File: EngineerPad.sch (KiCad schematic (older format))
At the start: 67 parts, among them J1 AVR ISP, SW1 SW_Push, SW10 SW_Push, SW11 SW_Push, SW12 SW_Push, SW13 SW_Push, SW14 SW_Push, SW15 SW_Push, SW16 SW_Push, SW17 SW_Push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

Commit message: switch to type a receptacle
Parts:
- removed Boot1: Boot, Button_Switch_THT:SW_PUSH_6mm, symbol Switch:SW_Push
- removed R3, R4: 5.1K, Resistor_THT:R_Axial_DIN0204_L3.6mm_D1.6mm_P5.08mm_Horizontal, symbol Device:R
- removed USB1: TYPE-C, JSA:USB_C_Receptacle_HRO_TYPE-C-31-M-12, symbol JSA:USB-2.0-Type-C-Receptacle
- added J2: USB_A, Connector_USB:USB_A_CONNFLY_DS1095-WNR0, symbol Connector:USB_A
- F1: footprint Fuse:Fuse_Bourns_MF-RG500 -> Fuse:Fuse_Bourns_MF-RHT050
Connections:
- net labels removed: Boot, CC1, CC2, DN, DP, VSUB
- wire segments 105 -> 86
- no-connect marks 7 -> 6

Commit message: socket and low profile
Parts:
- SW21, SW22, SW23: footprint Button_Switch_Keyboard:SW_Cherry_MX_1.00u_PCB -> JSA:SW_PG1350
- U1: footprint Package_DIP:DIP-28_W7.62mm -> Package_DIP:DIP-28_W7.62mm_Socket
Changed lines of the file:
@@
 F 0 "U1" H 1206 3746 50  0000 R CNN
 F 1 "ATmega328P-PU" H 1206 3655 50  0000 R CNN
-F 2 "Package_DIP:DIP-28_W7.62mm" H 1850 3700 50  0001 C CIN
+F 2 "Package_DIP:DIP-28_W7.62mm_Socket" H 1850 3700 50  0001 C CIN
 F 3 "http://ww1.microchip.com/downloads/en/DeviceDoc/ATmega328_P%20AVR%20MCU%20with%20picoPower%20Technology%20Data%20Sheet%2040001984A.pdf" H 1850 3700 50  0001 C CNN
 	1    1850 3700
@@
 F 0 "SW23" H 10550 4685 50  0000 C CNN
 F 1 "SW_Push" H 10550 4594 50  0000 C CNN
-F 2 "Button_Switch_Keyboard:SW_Cherry_MX_1.00u_PCB" H 10550 4600 50  0001 C CNN
+F 2 "JSA:SW_PG1350" H 10550 4600 50  0001 C CNN
 F 3 "~" H 10550 4600 50  0001 C CNN
 	1    10550 4400
@@
 F 0 "SW22" H 10050 4685 50  0000 C CNN
 F 1 "SW_Push" H 10050 4594 50  0000 C CNN
-F 2 "Button_Switch_Keyboard:SW_Cherry_MX_1.00u_PCB" H 10050 4600 50  0001 C CNN
+F 2 "JSA:SW_PG1350" H 10050 4600 50  0001 C CNN
 F 3 "~" H 10050 4600 50  0001 C CNN
 	1    10050 4400
@@
 F 0 "SW21" H 9550 4685 50  0000 C CNN
 F 1 "SW_Push" H 9550 4594 50  0000 C CNN
-F 2 "Button_Switch_Keyboard:SW_Cherry_MX_1.00u_PCB" H 9550 4600 50  0001 C CNN
+F 2 "JSA:SW_PG1350" H 9550 4600 50  0001 C CNN
 F 3 "~" H 9550 4600 50  0001 C CNN
 	1    9550 4400

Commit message: first layout
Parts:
- added R3: 1.5k, Resistor_THT:R_Axial_DIN0204_L3.6mm_D1.6mm_P5.08mm_Horizontal, symbol Device:R
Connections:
- net SCK is gone; now on net Row0: J1.3 (SCK), U1.19 (PB5)
- net SDI is gone; now on net Row2: J1.4 (SDI), U1.17 (PB3)
- net SDO is gone; now on net Row1: J1.1 (SDO), U1.18 (PB4)
- net +5V: now also R3.1
- net Col0: now also U1.27 (PC4); no longer U1.23 (PC0)
- net Col1: now also U1.26 (PC3); no longer U1.24 (PC1)
- net Col3: now also U1.24 (PC1); no longer U1.26 (PC3)
- net Col4: now also U1.23 (PC0); no longer U1.27 (PC4)
- net D+: now also U1.5 (PD3); no longer U1.4 (PD2)
- net D-: now also U1.4 (PD2); no longer U1.5 (PD3)
- net Row0: no longer U1.2 (PD0)
- net Row1: no longer U1.3 (PD1)
- net Row2: no longer U1.6 (PD4)
- net Row3: now also U1.16 (PB2); no longer U1.12 (PD6)
- net Row4: now also U1.15 (PB1); no longer U1.13 (PD7)
- net DN: now reaches D25.1 (K), J2.2 (D-), R2.2
- net DN: now also R3.2
- net DP: now reaches D24.1 (K), J2.3 (D+), R1.2
- no-connect marks 6 -> 10
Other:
- moved on the sheet: D25, R1, R2
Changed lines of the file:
@@
 $EndComp
 Text GLabel 4400 5200 2    50   Input ~ 0
-SCK
+Row0
 Text GLabel 4400 5100 2    50   Input ~ 0
-SDI
-Text GLabel 4400 5000 2    50   Input ~ 0
-SDO
-Text GLabel 2450 3000 2    50   Input ~ 0
-SCK
-Text GLabel 2450 2900 2    50   Input ~ 0
-SDO
+Row2
+Text GLabel 2450 2700 2    50   Input ~ 0
+Row3
 Text GLabel 2450 2800 2    50   Input ~ 0
-SDI
+Row2
 $Comp
 L power:+5V #PWR09
@@
 Col0
 Connection ~ 8850 1350
-Text GLabel 2450 4200 2    50   Input ~ 0
+Text GLabel 2450 3000 2    50   Input ~ 0
 Row0
-Text GLabel 2450 4300 2    50   Input ~ 0
+Text GLabel 2450 2900 2    50   Input ~ 0
 Row1
-Text GLabel 2450 3400 2    50   Input ~ 0
+Text GLabel 2450 3800 2    50   Input ~ 0
 Col0
-Text GLabel 2450 3500 2    50   Input ~ 0
+Text GLabel 2450 3700 2    50   Input ~ 0
 Col1
 NoConn ~ 2450 2500
-NoConn ~ 2450 2600
-NoConn ~ 2450 2700
 NoConn ~ 1250 2500
+Text GLabel 2450 4500 2    50   Input ~ 0
+D+
 Text GLabel 2450 4400 2    50   Input ~ 0
-D+
-Text GLabel 2450 4500 2    50   Input ~ 0
 D-
 Text Notes 6900 6250 0    50   ~ 0
@@
 Text GLabel 10350 850  1    50   Input ~ 0
 Col4
-Text GLabel 2450 4600 2    50   Input ~ 0
-Row2
-Text GLabel 2450 4800 2    50   Input ~ 0
-Row3
-Text GLabel 2450 4900 2    50   Input ~ 0
+Text GLabel 2450 2600 2    50   Input ~ 0
 Row4
 Text GLabel 2450 3600 2    50   Input ~ 0
 Col2
-Text GLabel 2450 3700 2    50   Input ~ 0
+Text GLabel 2450 3500 2    50   Input ~ 0
 Col3
-Text GLabel 2450 3800 2    50   Input ~ 0
+Text GLabel 2450 3400 2    50   Input ~ 0
 Col4
 Connection ~ 8350 1350
@@
 L Device:R R1
 U 1 1 5F4818C7
-P 6200 1850
-F 0 "R1" V 5993 1850 50  0000 C CNN
-F 1 "75" V 6084 1850 50  0000 C CNN
-F 2 "Resistor_THT:R_Axial_DIN0204_L3.6mm_D1.6mm_P5.08mm_Horizontal" V 6130 1850 50  0001 C CNN
-F 3 "~" H 6200 1850 50  0001 C CNN
-	1    6200 1850
+P 6550 1850
+F 0 "R1" V 6343 1850 50  0000 C CNN
+F 1 "75" V 6434 1850 50  0000 C CNN
+F 2 "Resistor_THT:R_Axial_DIN0204_L3.6mm_D1.6mm_P5.08mm_Horizontal" V 6480 1850 50  0001 C CNN
+F 3 "~" H 6550 1850 50  0001 C CNN
+	1    6550 1850
 	0    1    1    0
 $EndComp
@@
 L Device:R R2
 U 1 1 5F48290F
-P 6450 1950
-F 0 "R2" V 6243 1950 50  0000 C CNN
-F 1 "75" V 6334 1950 50  0000 C CNN
-F 2 "Resistor_THT:R_Axial_DIN0204_L3.6mm_D1.6mm_P5.08mm_Horizontal" V 6380 1950 50  0001 C CNN
-F 3 "~" H 6450 1950 50  0001 C CNN
-	1    6450 1950
+P 6800 1950
+F 0 "R2" V 6593 1950 50  0000 C CNN
+F 1 "75" V 6684 1950 50  0000 C CNN
+F 2 "Resistor_THT:R_Axial_DIN0204_L3.6mm_D1.6mm_P5.08mm_Horizontal" V 6730 1950 50  0001 C CNN
+F 3 "~" H 6800 1950 50  0001 C CNN
+	1    6800 1950
 	0    1    1    0
 $EndComp
@@
 	5650 1850 5950 1850
 Wire Wire Line
-	5650 1950 6250 1950
-Wire Wire Line
-	6350 1850 6900 1850
-Text GLabel 6900 1850 2    50   Input ~ 0
+	6700 1850 7250 1850
+Text GLabel 7250 1850 2    50   Input ~ 0
 D+
-Text GLabel 7100 1950 2    50   Input ~ 0
+Text GLabel 7450 1950 2    50   Input ~ 0
 D-
 Wire Wire Line
-	6600 1950 7100 1950
+	6950 1950 7450 1950
 $Comp
 L Device:D_Zener D25
 U 1 1 5F49960F
-P 6250 2100
-F 0 "D25" V 6204 2180 50  0000 L CNN
-F 1 "3.6V" V 6295 2180 50  0000 L CNN
-F 2 "Diode_THT:D_DO-35_SOD27_P7.62mm_Horizontal" H 6250 2100 50  0001 C CNN
-F 3 "~" H 6250 2100 50  0001 C CNN
-	1    6250 2100
+P 6600 2100
+F 0 "D25" V 6554 2180 50  0000 L CNN
+F 1 "3.6V" V 6645 2180 50  0000 L CNN
+F 2 "Diode_THT:D_DO-35_SOD27_P7.62mm_Horizontal" H 6600 2100 50  0001 C CNN
+F 3 "~" H 6600 2100 50  0001 C CNN
+	1    6600 2100
 	0    1    1    0
 $EndComp
@@
 	5950 2150 5950 2250
 Connection ~ 5950 1850
-Wire Wire Line
-	5950 1850 6050 1850
-Connection ~ 6250 1950
-Wire Wire Line
-	6250 1950 6300 1950
+Connection ~ 6600 1950
+Wire Wire Line
+	6600 1950 6650 1950
 Wire Wire Line
 	5250 2250 5350 2250
@@
 Connection ~ 5350 2250
 Connection ~ 5950 2250
-Wire Wire Line
-	5950 2250 6250 2250
 Wire Wire Line
 	5700 2250 5700 2400
@@
 Wire Wire Line
 	5800 1250 5800 1650
+Wire Wire Line
+	5800 1650 6050 1650
+$Comp
+L Device:R R3
+U 1 1 5F481387
+P 6300 1500
+F 0 "R3" H 6370 1546 50  0000 L CNN
+F 1 "1.5k" H 6370 1455 50  0000 L CNN
+F 2 "Resistor_THT:R_Axial_DIN0204_L3.6mm_D1.6mm_P5.08mm_Horizontal" V 6230 1500 50  0001 C CNN
+F 3 "~" H 6300 1500 50  0001 C CNN
+	1    6300 1500
+	1    0    0    -1
+$EndComp
+Wire Wire Line
+	5650 1950 6300 1950
+Wire Wire Line
+	5950 1850 6400 1850
+Wire Wire Line
+	5950 2250 6600 2250
+Wire Wire Line
+	6300 1650 6300 1950
+Connection ~ 6300 1950
+Wire Wire Line
+	6300 1950 6600 1950
+Wire Wire Line
+	6300 1350 6050 1350
+Connection ~ 6050 1350
 Connection ~ 5800 1650
-Wire Wire Line
-	5800 1650 6050 1650
+Text Label 5750 1850 0    50   ~ 0
+DP
+Text Label 5750 1950 0    50   ~ 0
+DN
+NoConn ~ 2450 4900
+NoConn ~ 9150 5350
+Text GLabel 4400 5000 2    50   Input ~ 0
+Row1
+NoConn ~ 2450 4200
+NoConn ~ 2450 4300
+NoConn ~ 2450 4600
+NoConn ~ 2450 4800
 $EndSCHEMATC

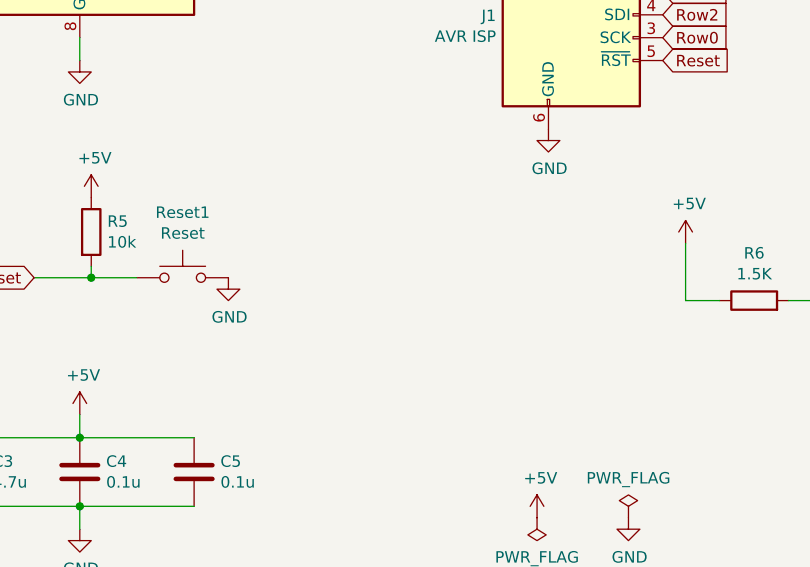
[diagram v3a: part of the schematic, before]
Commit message: Form factor 因為要做成5mm邊框切齊鍵帽，因此PCB從鍵帽處內縮1mm，外殼預計是5mm。
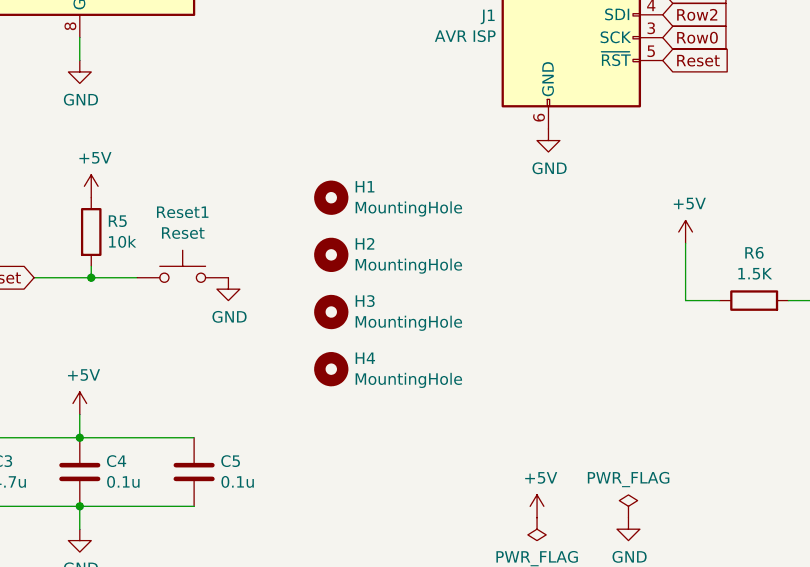
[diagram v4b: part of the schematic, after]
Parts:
- added H1, H2, H3, H4: MountingHole, MountingHole:MountingHole_2.2mm_M2, symbol Mechanical:MountingHole
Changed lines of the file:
@@
 Text GLabel 4400 5300 2    50   Input ~ 0
 Reset
-$Comp
-L JSA:Oshwa_ISP_6 J1
-U 1 1 5F1679A9
-P 4000 5200
-F 0 "J1" H 3671 5296 50  0000 R CNN
-F 1 "AVR ISP" H 3671 5205 50  0000 R CNN
-F 2 "JSA:AVRISP" V 3750 5250 50  0001 C CNN
-F 3 "https://www.oshwa.org/a-resolution-to-redefine-spi-signal-names" H 2725 4650 50  0001 C CNN
-	1    4000 5200
-	1    0    0    -1
-$EndComp
 Text GLabel 4400 5200 2    50   Input ~ 0
 Row0
@@
 NoConn ~ 2450 4600
 NoConn ~ 2450 4800
+$Comp
+L JSA:Oshwa_ISP_6 J1
+U 1 1 5F1679A9
+P 4000 5200
+F 0 "J1" H 3671 5296 50  0000 R CNN
+F 1 "AVR ISP" H 3671 5205 50  0000 R CNN
+F 2 "JSA:AVRISP" V 3750 5250 50  0001 C CNN
+F 3 "https://www.oshwa.org/a-resolution-to-redefine-spi-signal-names" H 2725 4650 50  0001 C CNN
+	1    4000 5200
+	1    0    0    -1
+$EndComp
+$Comp
+L Mechanical:MountingHole H1
+U 1 1 5F5595B1
+P 2950 5900
+F 0 "H1" H 3050 5946 50  0000 L CNN
+F 1 "MountingHole" H 3050 5855 50  0000 L CNN
+F 2 "MountingHole:MountingHole_2.2mm_M2" H 2950 5900 50  0001 C CNN
+F 3 "~" H 2950 5900 50  0001 C CNN
+	1    2950 5900
+	1    0    0    -1
+$EndComp
+$Comp
+L Mechanical:MountingHole H2
+U 1 1 5F55F584
+P 2950 6150
+F 0 "H2" H 3050 6196 50  0000 L CNN
+F 1 "MountingHole" H 3050 6105 50  0000 L CNN
+F 2 "MountingHole:MountingHole_2.2mm_M2" H 2950 6150 50  0001 C CNN
+F 3 "~" H 2950 6150 50  0001 C CNN
+	1    2950 6150
+	1    0    0    -1
+$EndComp
+$Comp
+L Mechanical:MountingHole H3
+U 1 1 5F5615B3
+P 2950 6400
+F 0 "H3" H 3050 6446 50  0000 L CNN
+F 1 "MountingHole" H 3050 6355 50  0000 L CNN
+F 2 "MountingHole:MountingHole_2.2mm_M2" H 2950 6400 50  0001 C CNN
+F 3 "~" H 2950 6400 50  0001 C CNN
+	1    2950 6400
+	1    0    0    -1
+$EndComp
+$Comp
+L Mechanical:MountingHole H4
+U 1 1 5F563758
+P 2950 6650
+F 0 "H4" H 3050 6696 50  0000 L CNN
+F 1 "MountingHole" H 3050 6605 50  0000 L CNN
+F 2 "MountingHole:MountingHole_2.2mm_M2" H 2950 6650 50  0001 C CNN
+F 3 "~" H 2950 6650 50  0001 C CNN
+	1    2950 6650
+	1    0    0    -1
+$EndComp
 $EndSCHEMATC

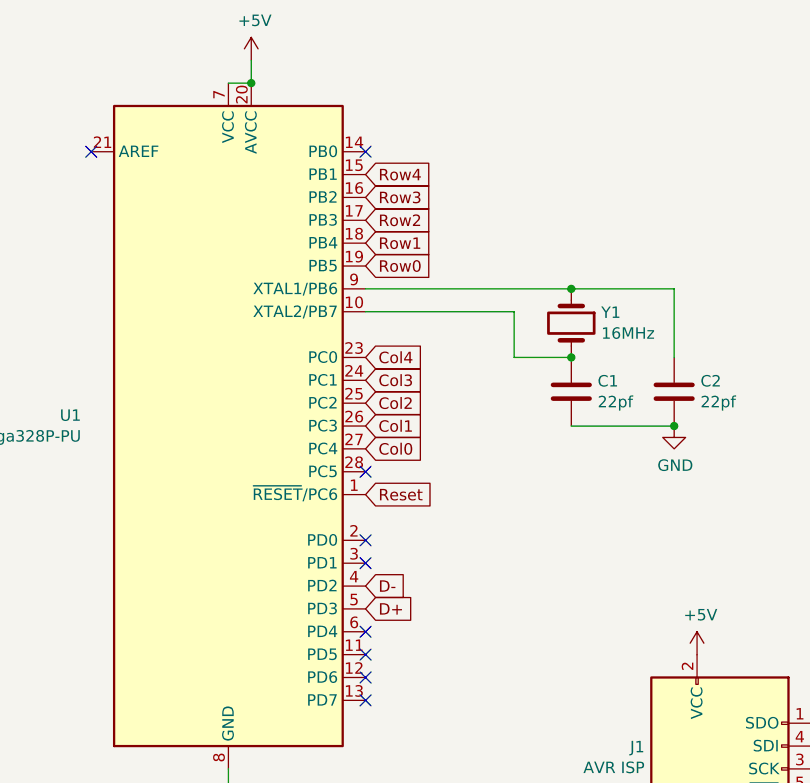
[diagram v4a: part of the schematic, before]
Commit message: inch based design
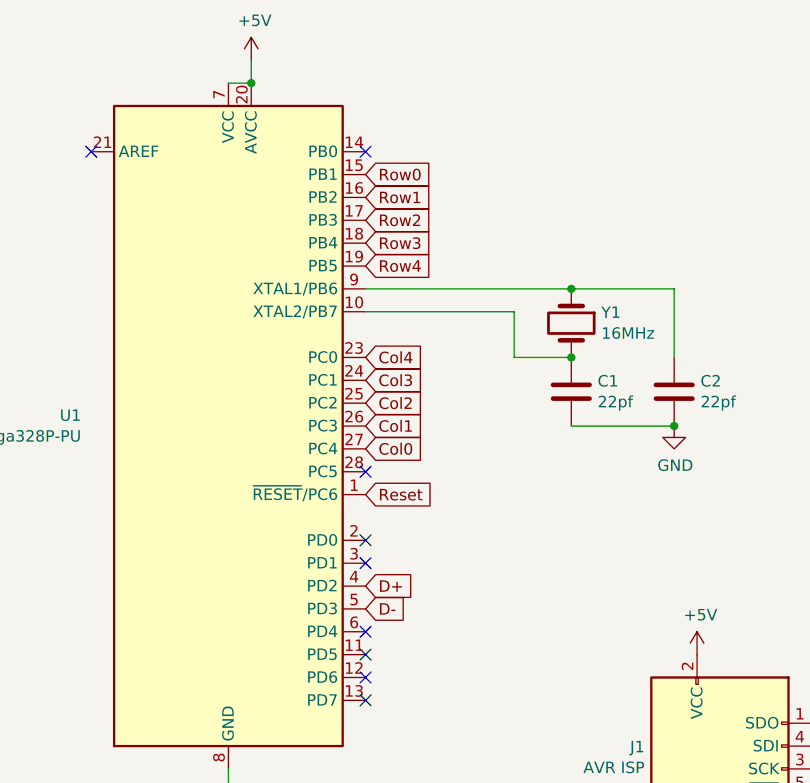
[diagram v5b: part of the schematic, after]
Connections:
- net D+: now also U1.4 (PD2); no longer U1.5 (PD3)
- net D-: now also U1.5 (PD3); no longer U1.4 (PD2)
- net Row0: now also U1.15 (PB1); no longer U1.19 (PB5)
- net Row1: now also U1.16 (PB2); no longer U1.18 (PB4)
- net Row3: now also U1.18 (PB4); no longer U1.16 (PB2)
- net Row4: now also U1.19 (PB5); no longer U1.15 (PB1)
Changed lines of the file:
@@
 Text GLabel 4400 5100 2    50   Input ~ 0
 Row2
-Text GLabel 2450 2700 2    50   Input ~ 0
+Text GLabel 2450 2900 2    50   Input ~ 0
 Row3
 Text GLabel 2450 2800 2    50   Input ~ 0
@@
 Col0
 Connection ~ 8850 1350
-Text GLabel 2450 3000 2    50   Input ~ 0
+Text GLabel 2450 2600 2    50   Input ~ 0
 Row0
-Text GLabel 2450 2900 2    50   Input ~ 0
+Text GLabel 2450 2700 2    50   Input ~ 0
 Row1
 Text GLabel 2450 3800 2    50   Input ~ 0
@@
 NoConn ~ 2450 2500
 NoConn ~ 1250 2500
+Text GLabel 2450 4400 2    50   Input ~ 0
+D+
 Text GLabel 2450 4500 2    50   Input ~ 0
-D+
-Text GLabel 2450 4400 2    50   Input ~ 0
 D-
 Text Notes 6900 6250 0    50   ~ 0
@@
 Text GLabel 10350 850  1    50   Input ~ 0
 Col4
-Text GLabel 2450 2600 2    50   Input ~ 0
+Text GLabel 2450 3000 2    50   Input ~ 0
 Row4
 Text GLabel 2450 3600 2    50   Input ~ 0

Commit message: wip
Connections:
- net Col0: now also J1.3 (SCK), U1.19 (PB5); no longer U1.27 (PC4)
- net Col1: now also J1.1 (SDO), U1.18 (PB4); no longer U1.26 (PC3)
- net Col2: now also J1.4 (SDI), U1.17 (PB3); no longer U1.25 (PC2)
- net Col3: now also U1.16 (PB2); no longer U1.24 (PC1)
- net Col4: now also U1.15 (PB1); no longer U1.23 (PC0)
- net Row0: now also U1.23 (PC0); no longer J1.3 (SCK), U1.15 (PB1)
- net Row1: now also U1.24 (PC1); no longer J1.1 (SDO), U1.16 (PB2)
- net Row2: now also U1.25 (PC2); no longer J1.4 (SDI), U1.17 (PB3)
- net Row3: now also U1.26 (PC3); no longer U1.18 (PB4)
- net Row4: now also U1.27 (PC4); no longer U1.19 (PB5)
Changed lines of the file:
@@
 Reset
 Text GLabel 4400 5200 2    50   Input ~ 0
-Row0
+Col0
 Text GLabel 4400 5100 2    50   Input ~ 0
-Row2
-Text GLabel 2450 2900 2    50   Input ~ 0
+Col2
+Text GLabel 2450 3700 2    50   Input ~ 0
 Row3
-Text GLabel 2450 2800 2    50   Input ~ 0
+Text GLabel 2450 3600 2    50   Input ~ 0
 Row2
 $Comp
@@
 Col0
 Connection ~ 8850 1350
-Text GLabel 2450 2600 2    50   Input ~ 0
+Text GLabel 2450 3400 2    50   Input ~ 0
 Row0
-Text GLabel 2450 2700 2    50   Input ~ 0
+Text GLabel 2450 3500 2    50   Input ~ 0
 Row1
-Text GLabel 2450 3800 2    50   Input ~ 0
+Text GLabel 2450 3000 2    50   Input ~ 0
 Col0
-Text GLabel 2450 3700 2    50   Input ~ 0
+Text GLabel 2450 2900 2    50   Input ~ 0
 Col1
 NoConn ~ 2450 2500
@@
 Text GLabel 10350 850  1    50   Input ~ 0
 Col4
-Text GLabel 2450 3000 2    50   Input ~ 0
+Text GLabel 2450 3800 2    50   Input ~ 0
 Row4
-Text GLabel 2450 3600 2    50   Input ~ 0
+Text GLabel 2450 2800 2    50   Input ~ 0
 Col2
-Text GLabel 2450 3500 2    50   Input ~ 0
+Text GLabel 2450 2700 2    50   Input ~ 0
 Col3
-Text GLabel 2450 3400 2    50   Input ~ 0
+Text GLabel 2450 2600 2    50   Input ~ 0
 Col4
 Connection ~ 8350 1350
@@
 NoConn ~ 9150 5350
 Text GLabel 4400 5000 2    50   Input ~ 0
-Row1
+Col1
 NoConn ~ 2450 4200
 NoConn ~ 2450 4300

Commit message: handwired
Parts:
- added J?: AVR-ISP-6, symbol Connector:AVR-ISP-6
- J1: value AVR ISP -> AVR ISP 6
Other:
- moved on the sheet: J1
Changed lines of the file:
@@
 L power:+5V #PWR04
 U 1 1 5F169608
-P 3900 4700
-F 0 "#PWR04" H 3900 4550 50  0001 C CNN
-F 1 "+5V" H 3915 4873 50  0000 C CNN
-F 2 "" H 3900 4700 50  0001 C CNN
-F 3 "" H 3900 4700 50  0001 C CNN
-	1    3900 4700
-	1    0    0    -1
+P 3400 1700
+F 0 "#PWR04" H 3400 1550 50  0001 C CNN
+F 1 "+5V" H 3415 1873 50  0000 C CNN
+F 2 "" H 3400 1700 50  0001 C CNN
+F 3 "" H 3400 1700 50  0001 C CNN
+	1    3400 1700
+	0    1    1    0
 $EndComp
 $Comp
 L power:GND #PWR07
 U 1 1 5F169EF0
-P 3900 5600
-F 0 "#PWR07" H 3900 5350 50  0001 C CNN
-F 1 "GND" H 3905 5427 50  0000 C CNN
-F 2 "" H 3900 5600 50  0001 C CNN
-F 3 "" H 3900 5600 50  0001 C CNN
-	1    3900 5600
-	1    0    0    -1
+P 2500 1700
+F 0 "#PWR07" H 2500 1450 50  0001 C CNN
+F 1 "GND" H 2505 1527 50  0000 C CNN
+F 2 "" H 2500 1700 50  0001 C CNN
+F 3 "" H 2500 1700 50  0001 C CNN
+	1    2500 1700
+	0    1    1    0
 $EndComp
 $Comp
@@
 	1    0    0    -1
 $EndComp
-Text GLabel 4400 5300 2    50   Input ~ 0
+Text GLabel 2800 2200 3    50   Input ~ 0
 Reset
-Text GLabel 4400 5200 2    50   Input ~ 0
-Col0
-Text GLabel 4400 5100 2    50   Input ~ 0
-Col2
 Text GLabel 2450 3700 2    50   Input ~ 0
 Row3
@@
 Text GLabel 2450 3500 2    50   Input ~ 0
 Row1
-Text GLabel 2450 3000 2    50   Input ~ 0
+Text GLabel 3850 3000 2    50   Input ~ 0
 Col0
-Text GLabel 2450 2900 2    50   Input ~ 0
+Text GLabel 3850 2900 2    50   Input ~ 0
 Col1
 NoConn ~ 2450 2500
@@
 Text GLabel 2450 3800 2    50   Input ~ 0
 Row4
-Text GLabel 2450 2800 2    50   Input ~ 0
+Text GLabel 3850 2800 2    50   Input ~ 0
 Col2
-Text GLabel 2450 2700 2    50   Input ~ 0
+Text GLabel 3850 2700 2    50   Input ~ 0
 Col3
-Text GLabel 2450 2600 2    50   Input ~ 0
+Text GLabel 3850 2600 2    50   Input ~ 0
 Col4
 Connection ~ 8350 1350
@@
 NoConn ~ 2450 4900
 NoConn ~ 9150 5350
-Text GLabel 4400 5000 2    50   Input ~ 0
-Col1
 NoConn ~ 2450 4200
 NoConn ~ 2450 4300
@@
 L JSA:Oshwa_ISP_6 J1
 U 1 1 5F1679A9
-P 4000 5200
-F 0 "J1" H 3671 5296 50  0000 R CNN
-F 1 "AVR ISP" H 3671 5205 50  0000 R CNN
-F 2 "JSA:AVRISP" V 3750 5250 50  0001 C CNN
-F 3 "https://www.oshwa.org/a-resolution-to-redefine-spi-signal-names" H 2725 4650 50  0001 C CNN
-	1    4000 5200
-	1    0    0    -1
+P 2900 1800
+F 0 "J1" H 2571 1896 50  0000 R CNN
+F 1 "AVR ISP 6" V 2571 1805 50  0000 C CNN
+F 2 "JSA:AVRISP" V 2650 1850 50  0001 C CNN
+F 3 "https://www.oshwa.org/a-resolution-to-redefine-spi-signal-names" H 1625 1250 50  0001 C CNN
+	1    2900 1800
+	0    1    1    0
 $EndComp
 $Comp
@@
 	1    0    0    -1
 $EndComp
+Wire Wire Line
+	2900 2200 2900 3000
+Wire Wire Line
+	2900 3000 2450 3000
+Wire Wire Line
+	3000 2200 3000 2800
+Wire Wire Line
+	3000 2800 2450 2800
+Wire Wire Line
+	3100 2200 3100 2900
+Wire Wire Line
+	3100 2900 2450 2900
+Wire Wire Line
+	2900 3000 3850 3000
+Connection ~ 2900 3000
+Wire Wire Line
+	3100 2900 3850 2900
+Connection ~ 3100 2900
+Wire Wire Line
+	3000 2800 3850 2800
+Connection ~ 3000 2800
+Wire Wire Line
+	2450 2700 3850 2700
+Wire Wire Line
+	2450 2600 3850 2600
+$Comp
+L Connector:AVR-ISP-6 J?
+U 1 1 5F4E2942
+P 4050 1800
+F 0 "J?" V 3583 1850 50  0000 C CNN
+F 1 "AVR-ISP-6" V 3674 1850 50  0000 C CNN
+F 2 "" V 3800 1850 50  0001 C CNN
+F 3 " ~" H 2775 1250 50  0001 C CNN
+	1    4050 1800
+	0    1    1    0
+$EndComp
 $EndSCHEMATC
